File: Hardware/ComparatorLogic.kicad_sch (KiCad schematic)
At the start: 68 parts

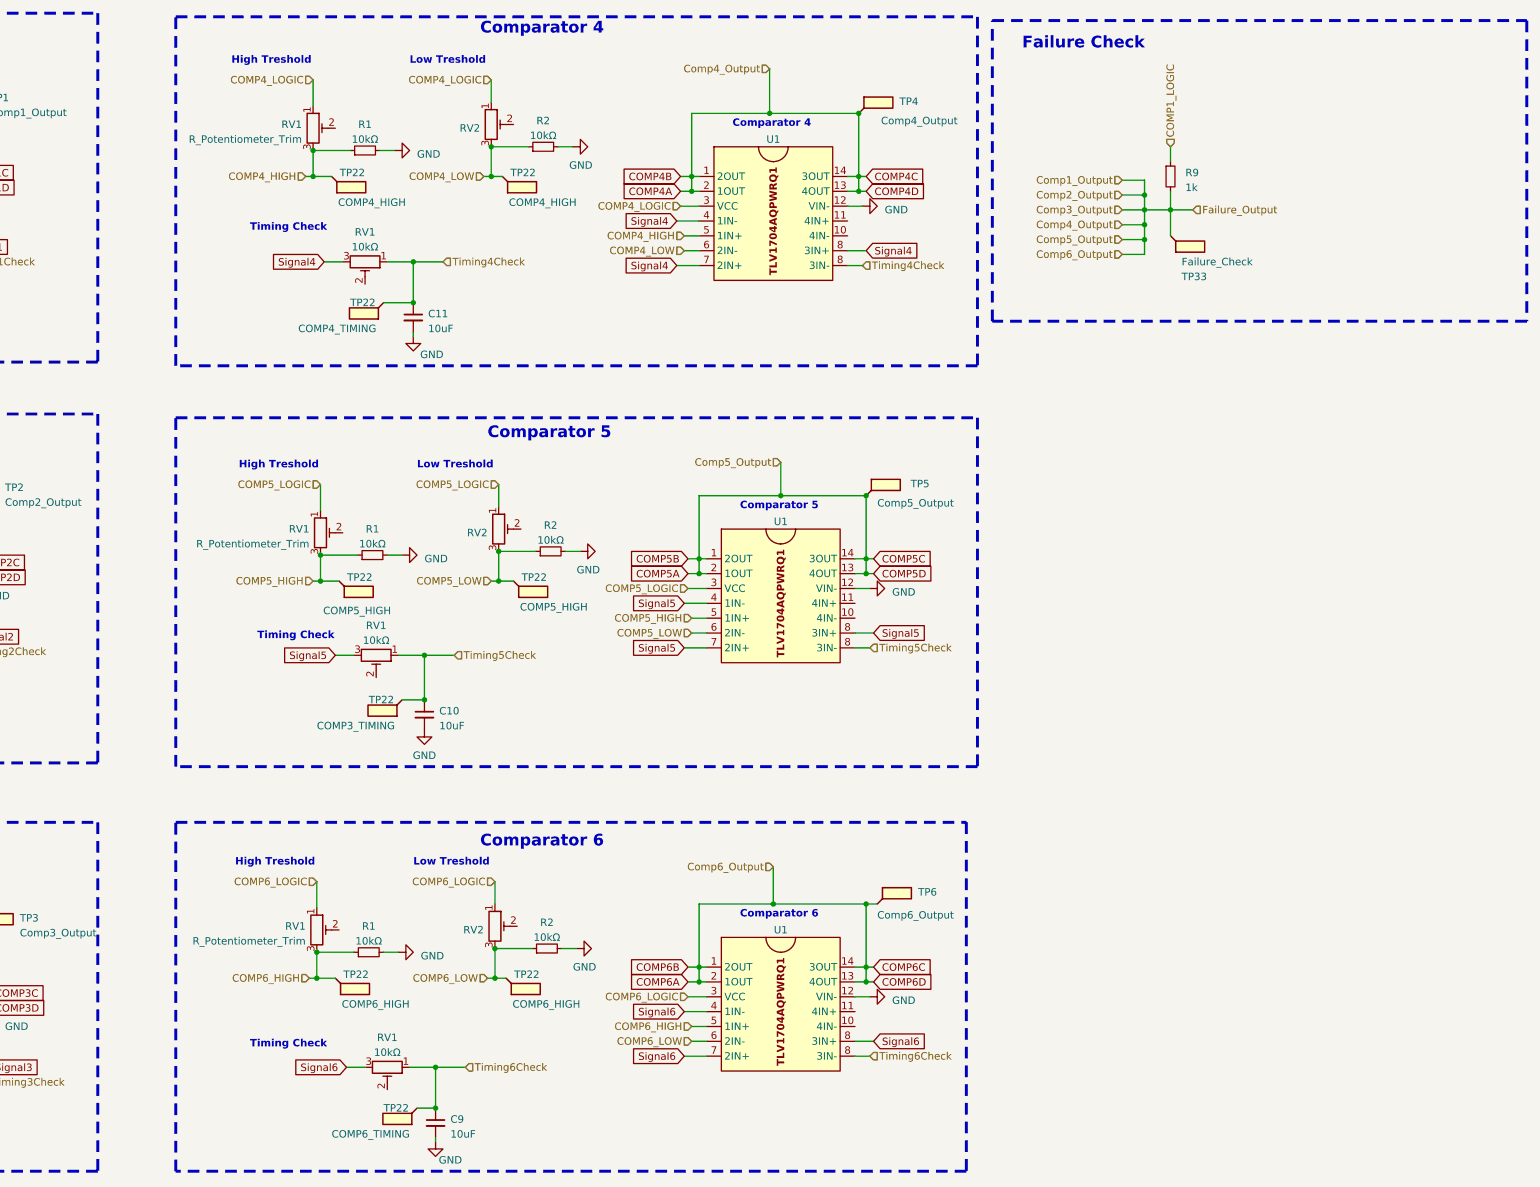
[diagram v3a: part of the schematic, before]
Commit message: Added dip switch for comparator active selection
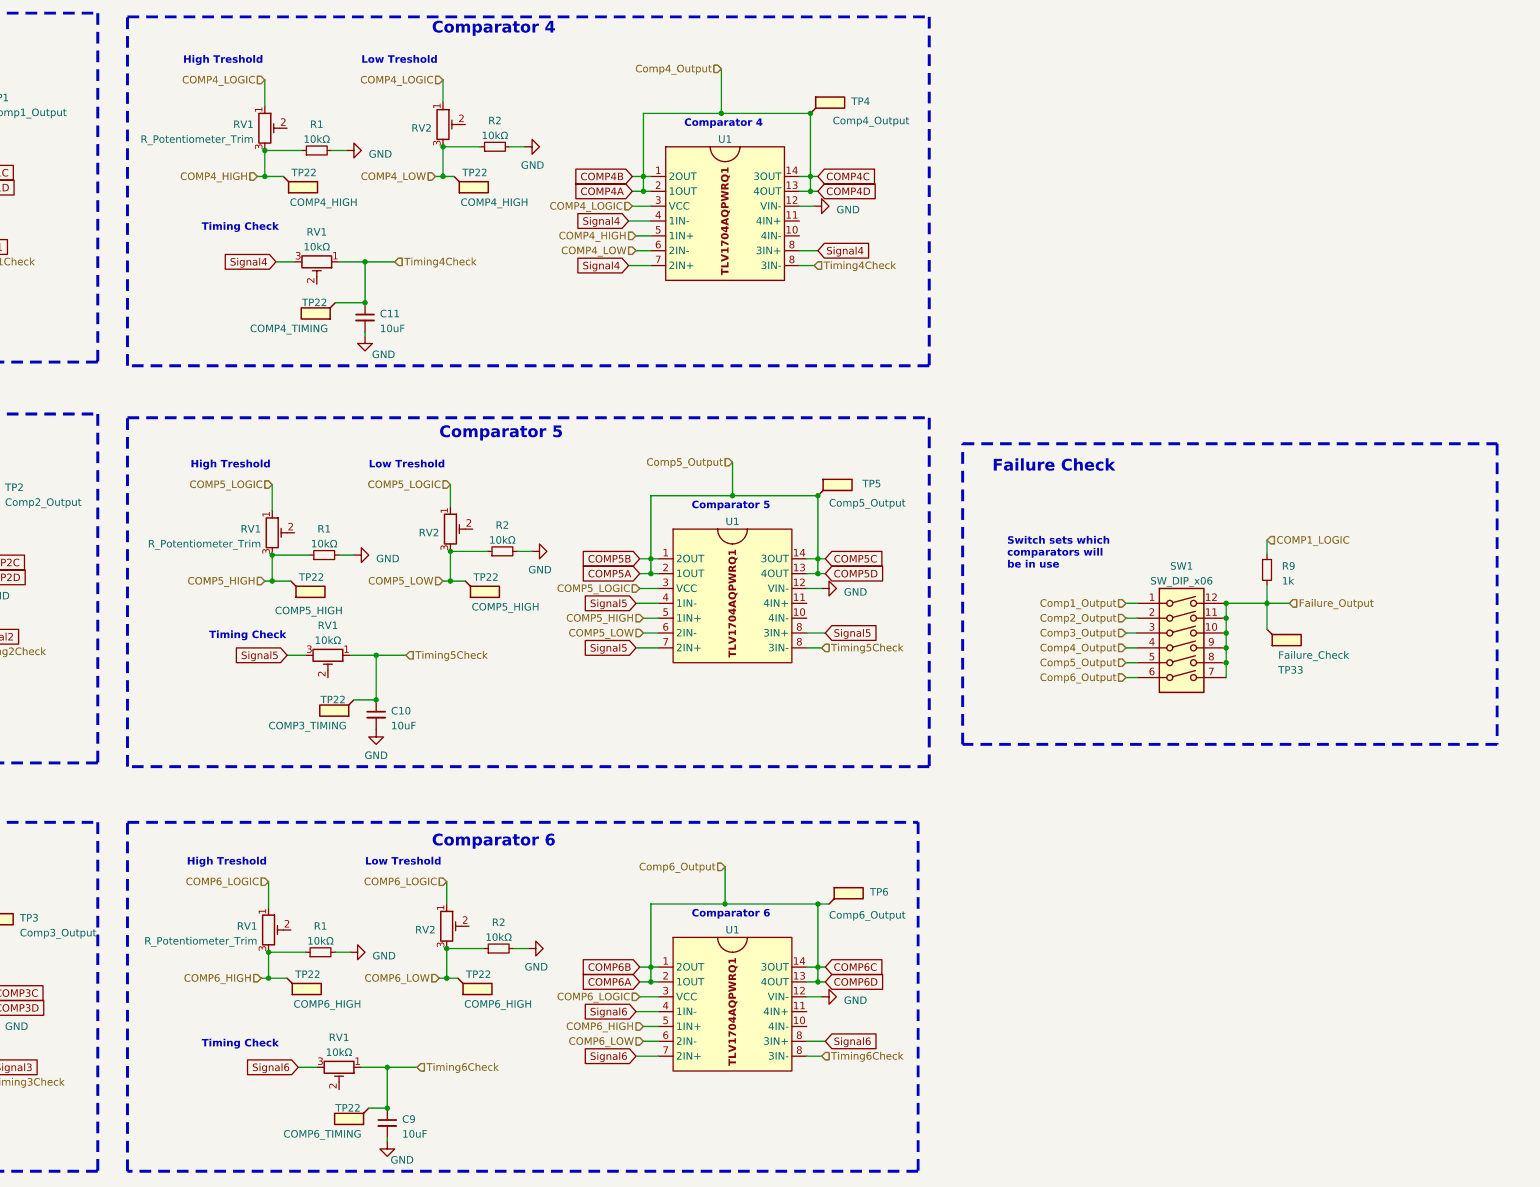
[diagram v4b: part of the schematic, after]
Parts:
- added SW1: SW_DIP_x06, Button_Switch_THT:418117270906, symbol Switch:SW_DIP_x06
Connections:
- net COMP1A: now also SW1.1; no longer R9.2, TP2.1, TP3.1, TP33.1, TP4.1, TP5.1, TP6.1, U1.1 (2OUT), U1.1 (2OUT), U1.1 (2OUT), U1.1 (2OUT), U1.1 (2OUT), U1.13 (4OUT), U1.13 (4OUT), U1.13 (4OUT), U1.13 (4OUT), U1.13 (4OUT), U1.14 (3OUT), U1.14 (3OUT), U1.14 (3OUT), U1.14 (3OUT), U1.14 (3OUT), U1.2 (1OUT), U1.2 (1OUT), U1.2 (1OUT), U1.2 (1OUT), U1.2 (1OUT)
- new net COMP2A: SW1.2, TP2.1, U1.1 (2OUT), U1.13 (4OUT), U1.14 (3OUT), U1.2 (1OUT)
- new net COMP3A: SW1.3, TP3.1, U1.1 (2OUT), U1.13 (4OUT), U1.14 (3OUT), U1.2 (1OUT)
- new net COMP4A: SW1.4, TP4.1, U1.1 (2OUT), U1.13 (4OUT), U1.14 (3OUT), U1.2 (1OUT)
- new net COMP5A: SW1.5, TP5.1, U1.1 (2OUT), U1.13 (4OUT), U1.14 (3OUT), U1.2 (1OUT)
- new net COMP6A: SW1.6, TP6.1, U1.1 (2OUT), U1.13 (4OUT), U1.14 (3OUT), U1.2 (1OUT)
- new net Failure_Output: R9.2, SW1.10, SW1.11, SW1.12, SW1.7, SW1.8, SW1.9, TP33.1
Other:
- note added: "Switch sets which comparators will be in use"
- moved on the sheet: C10, C11, C9, R1, R2, R9, RV1, RV2, TP22, TP33, TP4, TP5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
